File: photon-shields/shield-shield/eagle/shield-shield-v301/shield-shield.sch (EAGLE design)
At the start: 42 parts, among them IC1 MC33269D-5.0, IC2 74ABT125PW, J1 POWER_JACKSLT, Q1 MOSFET-NCHANNELBSS138, Q2 MOSFET-NCHANNELBSS138

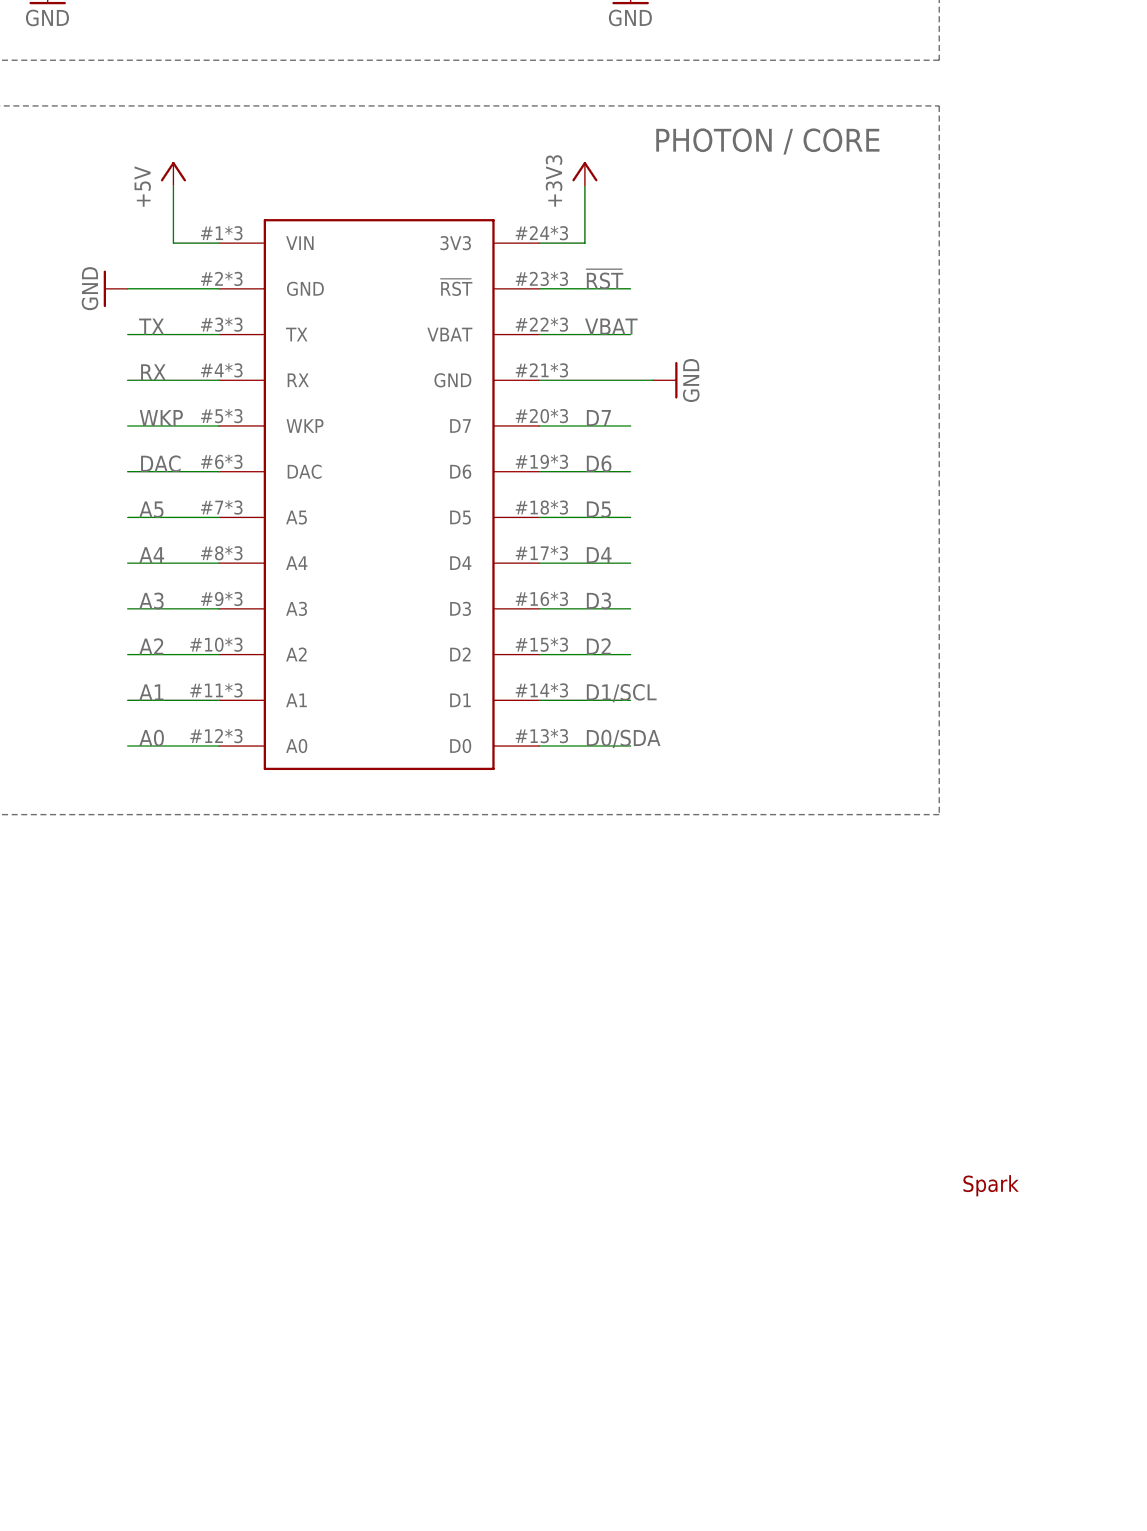
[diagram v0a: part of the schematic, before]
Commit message: added rev numbers to schematic sheets and regenerated the PDFs
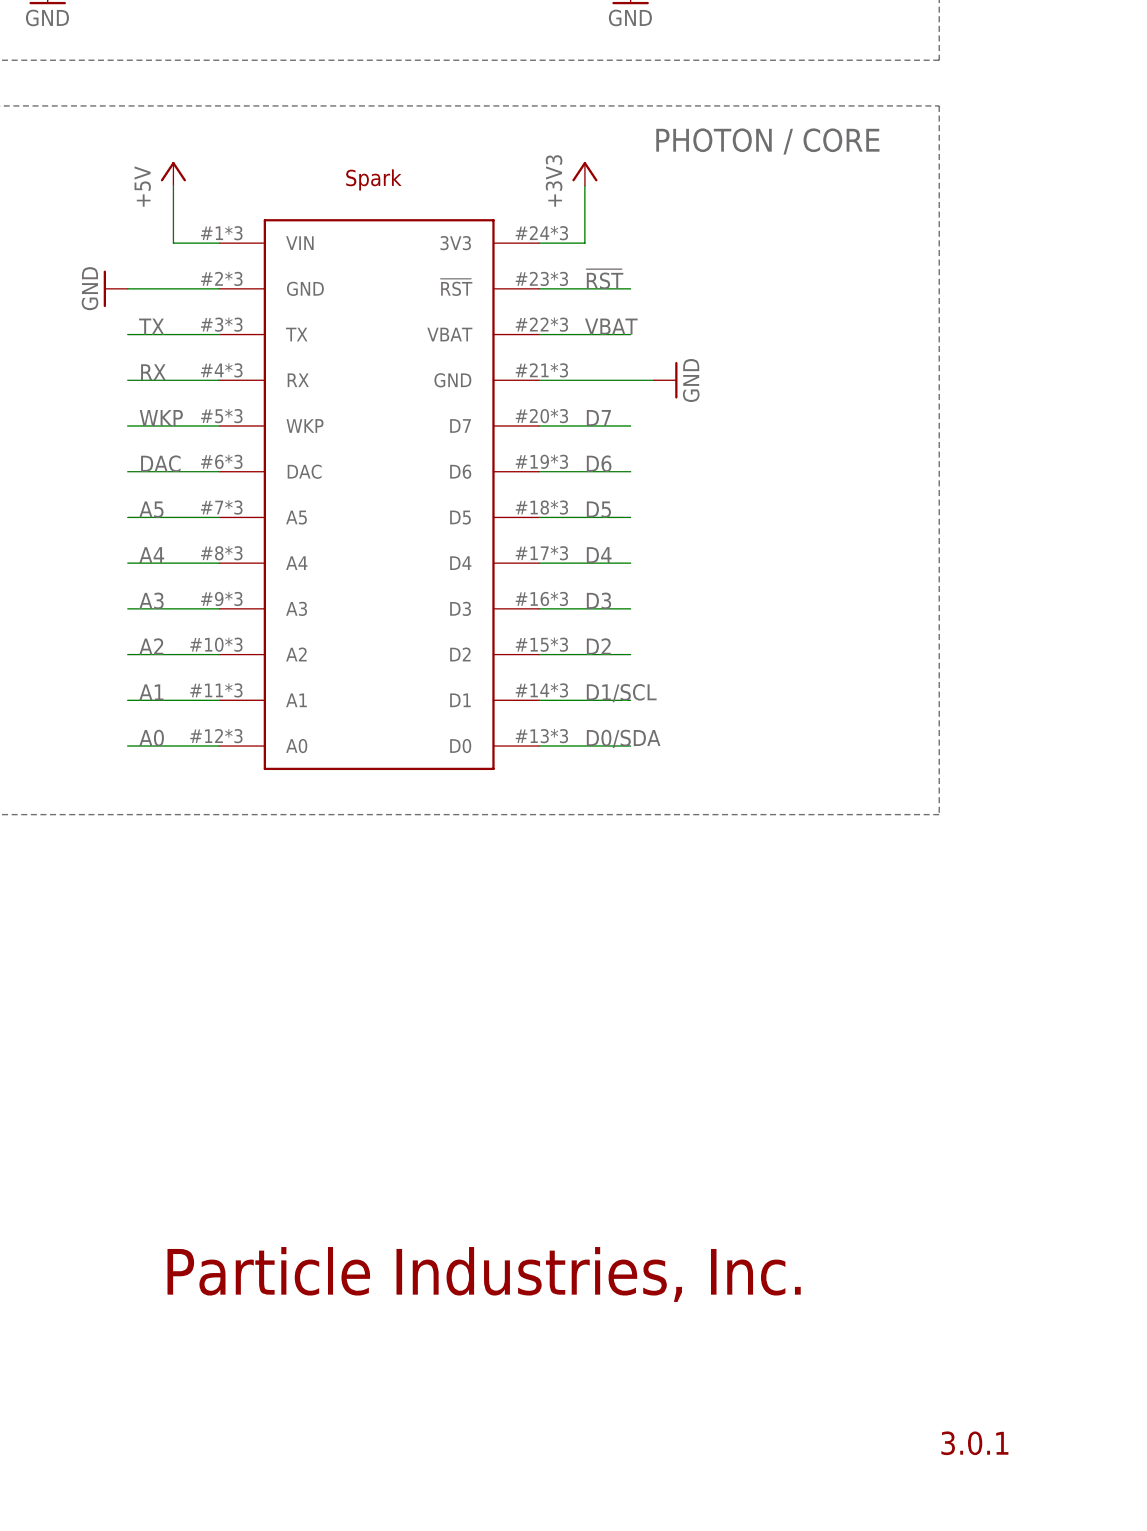
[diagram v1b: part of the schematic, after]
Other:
- note added: "3.0.1"
- note added: "Particle Industries, Inc."
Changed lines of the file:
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@@
 <setting verticaltext="up"/>
 </settings>
-<grid distance="0.1" unitdist="inch" unit="inch" style="lines" multiple="1" display="yes" altdistance="0.01" altunitdist="inch" altunit="inch"/>
+<grid distance="0.1" unitdist="inch" unit="inch" style="lines" multiple="1" display="no" altdistance="0.01" altunitdist="inch" altunit="inch"/>
 <layers>
 <layer number="1" name="Top" color="4" fill="1" visible="no" active="no"/>
@@
 <text x="207.01" y="165.1" size="2.54" layer="95" font="vector">3V3 -&gt; 5V</text>
 <text x="344.17" y="152.4" size="2.54" layer="95" font="vector">PHOTON / CORE</text>
+<text x="375.92" y="7.62" size="2.54" layer="94">3.0.1</text>
+<text x="289.56" y="25.4" size="5.08" layer="94">Particle Industries, Inc.</text>
 </plain>
 <instances>
@@
 <instance part="JP9" gate="G$1" x="146.05" y="200.66"/>
 <instance part="JP10" gate="G$1" x="205.74" y="200.66" rot="MR0"/>
-<instance part="U$2" gate="G$1" x="378.46" y="36.83"/>
+<instance part="U$2" gate="G$1" x="309.88" y="148.59"/>
 <instance part="JP11" gate="G$1" x="194.31" y="240.03" smashed="yes" rot="R180">
 <attribute name="NAME" x="196.85" y="236.728" size="1.778" layer="95" rot="R180"/>
